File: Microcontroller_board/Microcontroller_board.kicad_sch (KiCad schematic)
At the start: 0 parts

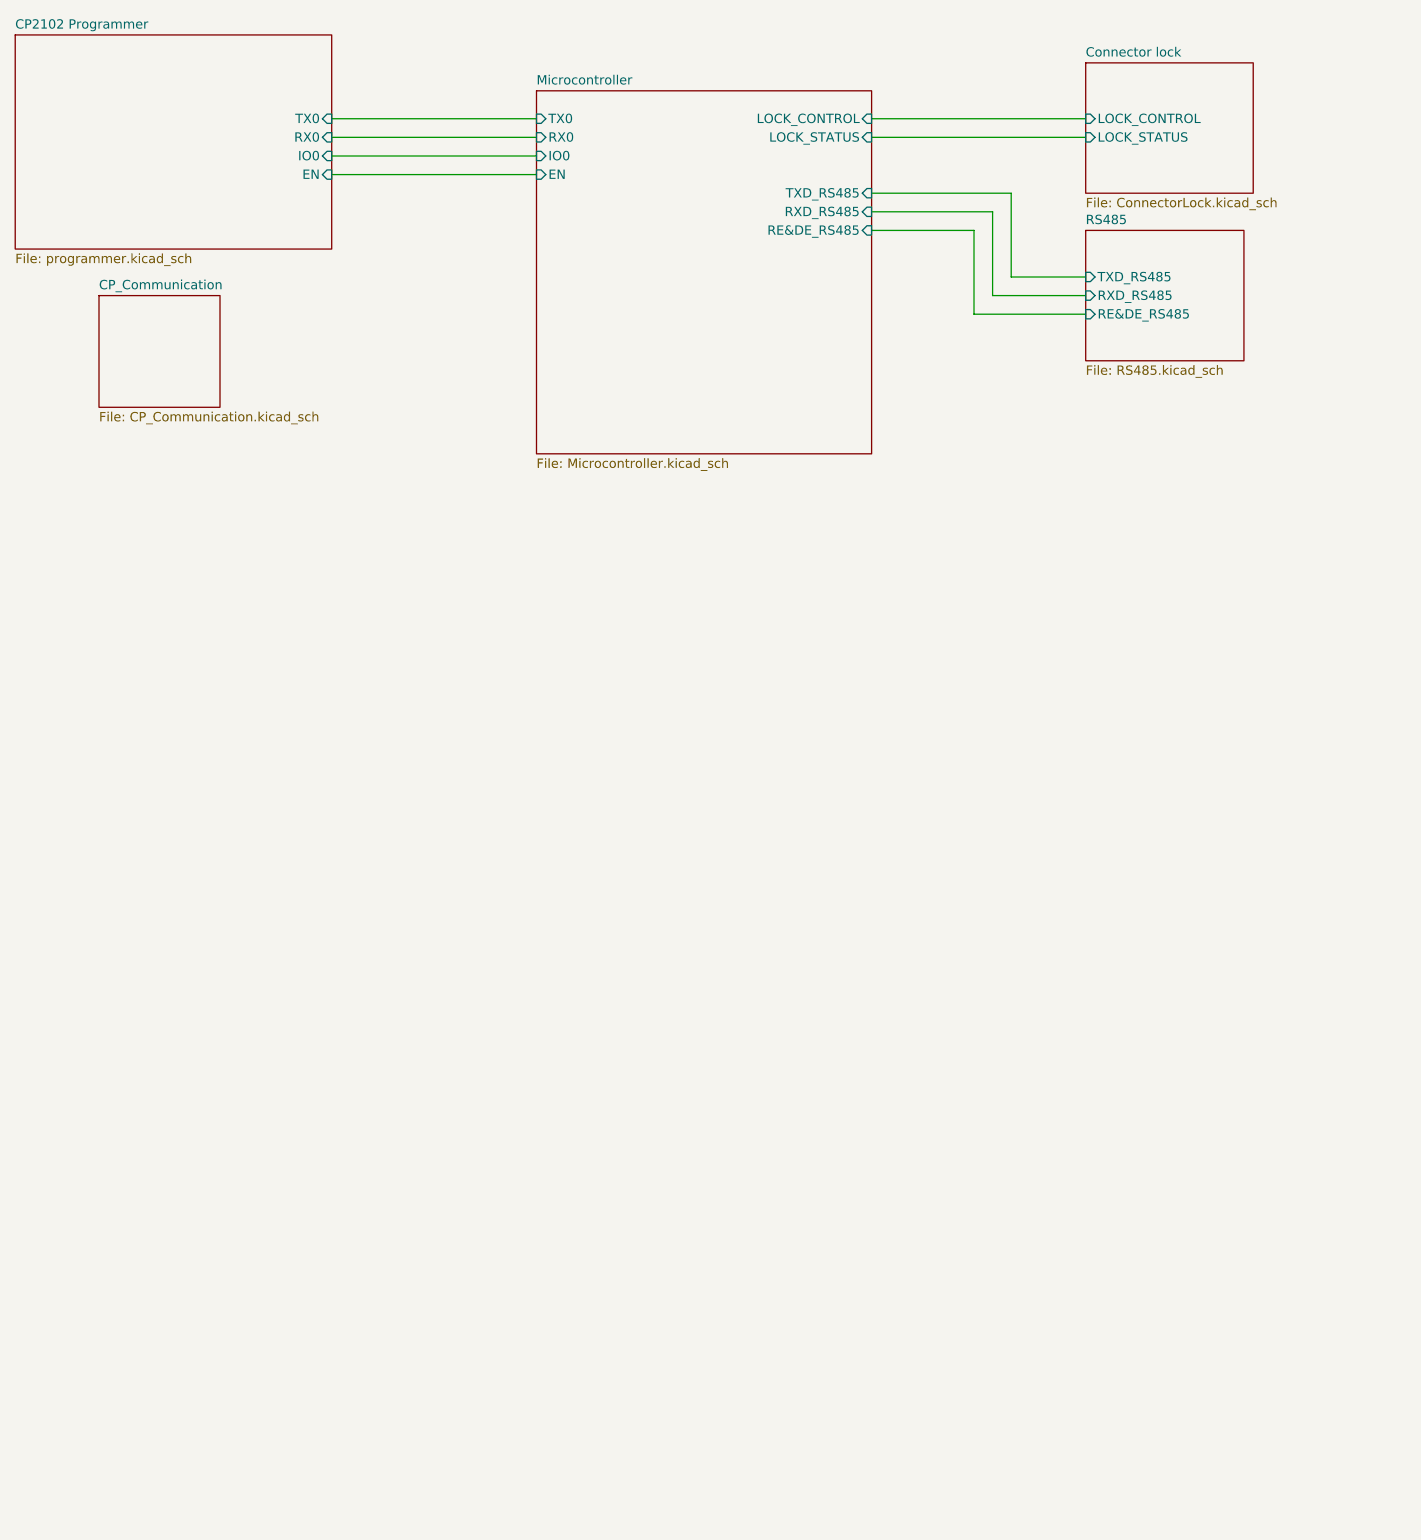
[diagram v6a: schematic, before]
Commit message: Delete sensingboard project and add stm32 micro to the schematic
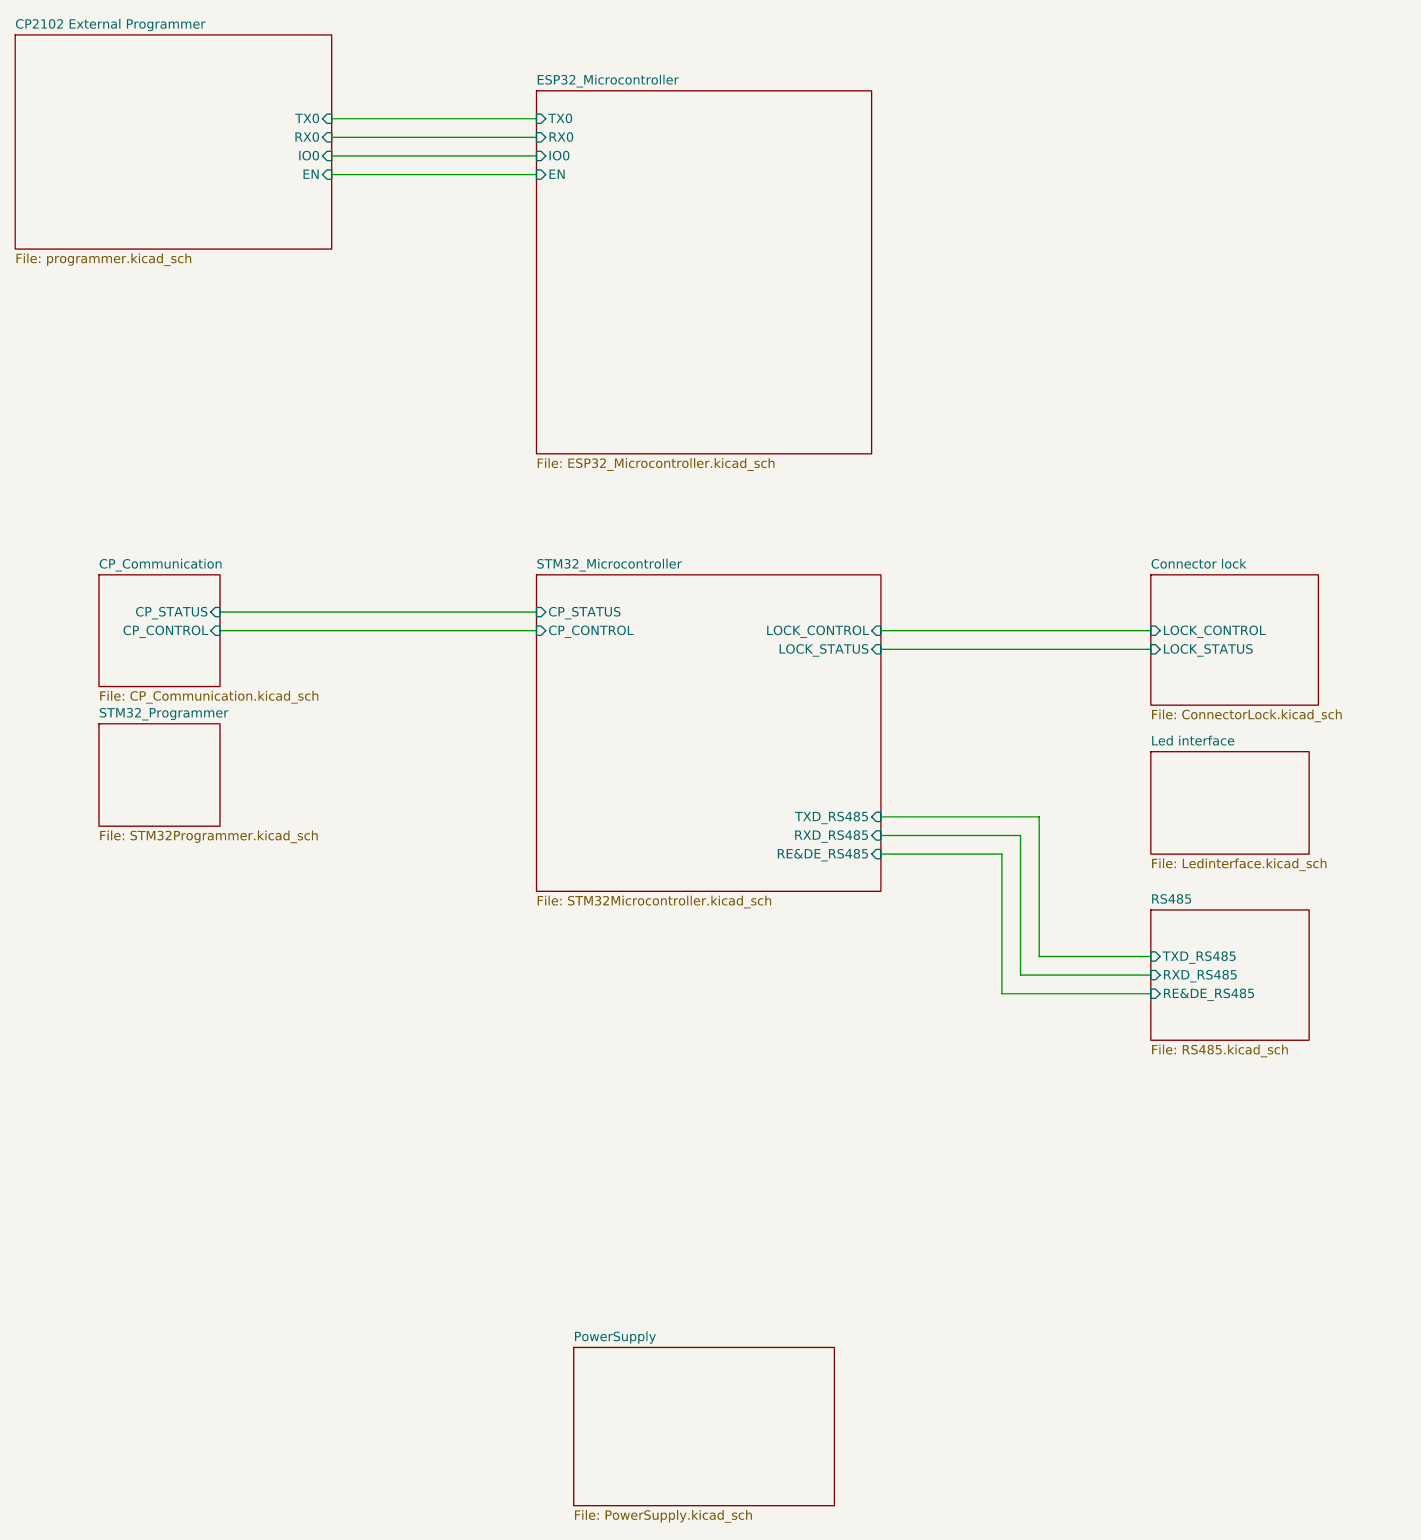
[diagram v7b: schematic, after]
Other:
- sheet CP2102 Programmer renamed CP2102 External Programmer
- sheet Microcontroller renamed ESP32_Microcontroller
- added sheet Led interface (Ledinterface.kicad_sch)
- added sheet PowerSupply (PowerSupply.kicad_sch)
- added sheet STM32_Microcontroller (STM32Microcontroller.kicad_sch)
- added sheet STM32_Programmer (STM32Programmer.kicad_sch)
- sheet CP_Communication ports: added CP_CONTROL, CP_STATUS; removed none
- sheet ESP32_Microcontroller: file Microcontroller.kicad_sch -> ESP32_Microcontroller.kicad_sch
- sheet ESP32_Microcontroller ports: added none; removed LOCK_CONTROL, LOCK_STATUS, RE&DE_RS485, RXD_RS485, TXD_RS485

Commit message: Upload
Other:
- sheet CP2102 External Programmer renamed CP2102 Programmer Connector
- sheet STM32_Programmer ports: added SWCLK, SWD, SWDIO; removed none
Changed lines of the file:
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@@
       (effects (font (size 1.27 1.27)) (justify left top))
+    )
+    (pin "SWCLK" input (at 135.89 127 0)
+      (effects (font (size 1.27 1.27)) (justify right))
+    )
+    (pin "SWDIO" input (at 135.89 129.54 0)
+      (effects (font (size 1.27 1.27)) (justify right))
+    )
+    (pin "SWD" input (at 135.89 132.08 0)
+      (effects (font (size 1.27 1.27)) (justify right))
     )
     (instances
@@
     (stroke (width 0.1524) (type solid))
     (fill (color 0 0 0 0.0000))
-    (property "Sheetname" "CP2102 External Programmer" (at 107.95 29.7684 0)
+    (property "Sheetname" "CP2102 Programmer Connector" (at 107.95 29.7684 0)
       (effects (font (size 1.27 1.27)) (justify left bottom))
     )
